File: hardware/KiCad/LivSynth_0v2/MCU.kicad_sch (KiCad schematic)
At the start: 20 parts, among them J16 USB_B_Micro, J19 SWD, SW7 SW_SPDT, U9 STM32F405RGT6, Y1 ABM8-16

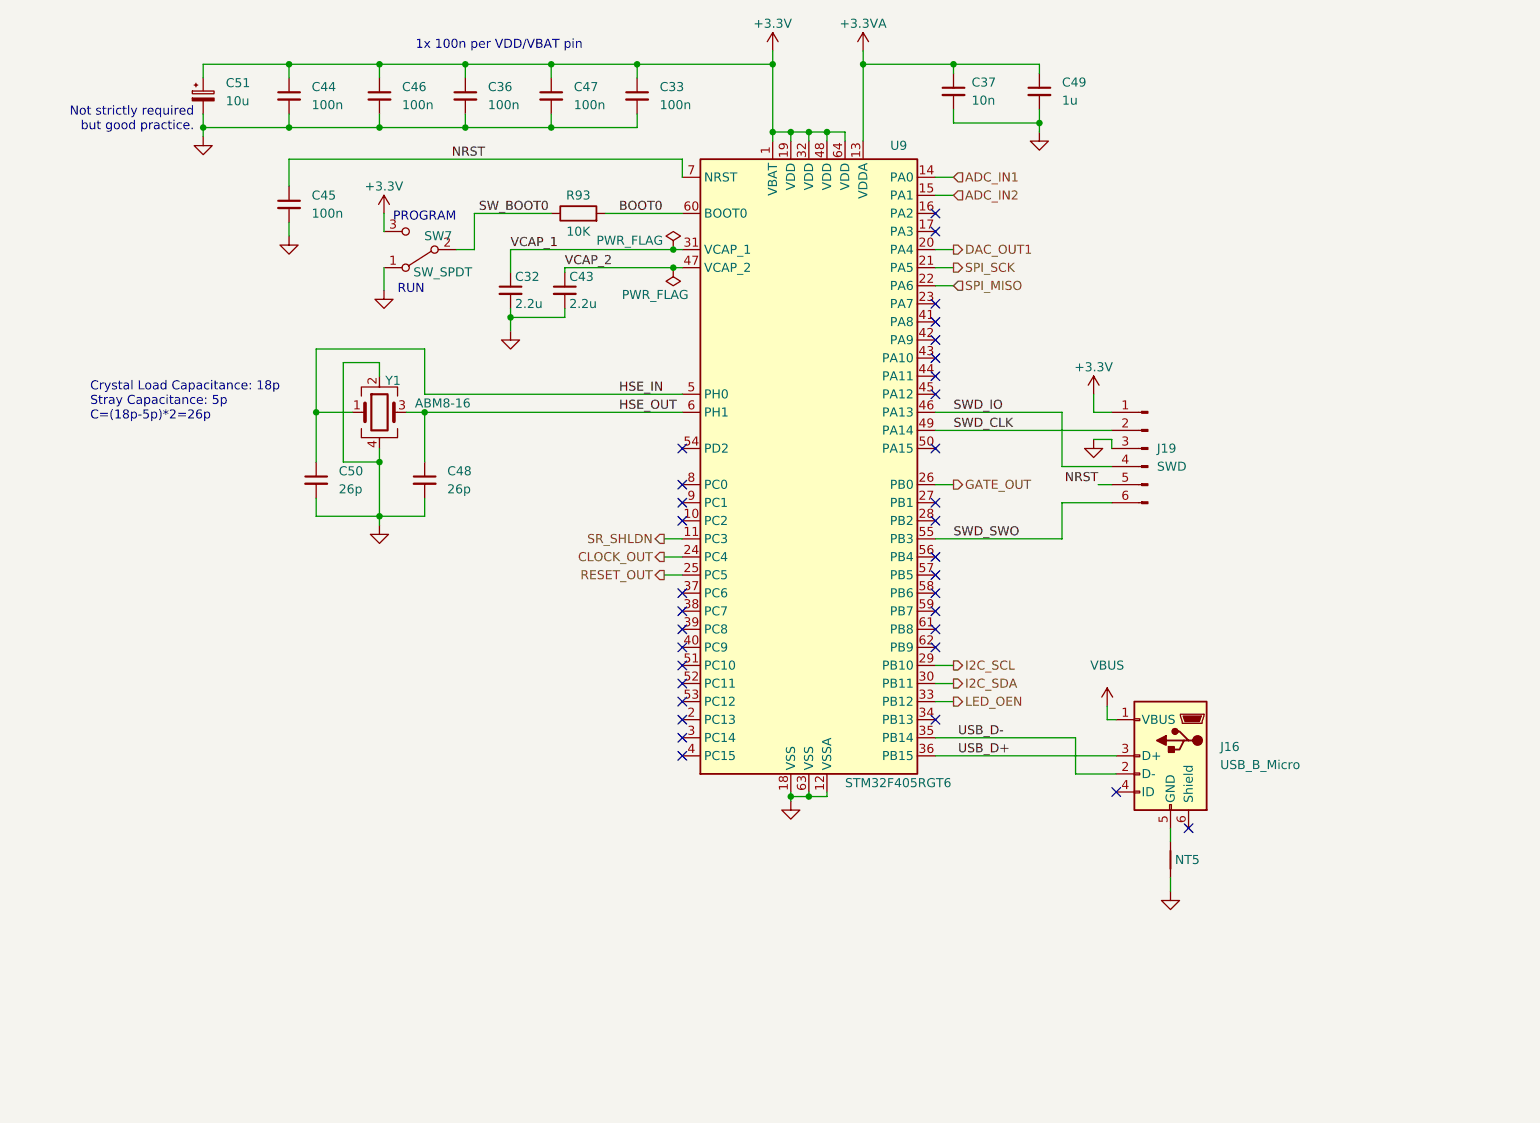
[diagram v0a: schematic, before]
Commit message: Analog redesign:  - Power: Add voltage and current test points  - MCU: use PA11/PA12 for USB DFU interface  - MCU: add NRST reset switch  - Slew: increase portamento cap  - VCO: invert trim pots  - VCF: let resonance kick in earlier  - VCF: invert pots  - VCA: invert trim pot  - EG: full redesign, properly referencing VGND now  - LFO: R61 = 51K  - ModMatrix: add EG attenuverters  - IO: invert pots  - IO: limit output gain for 1W speaker  - IO: connect BTN_SHIFT in gap free order to SR
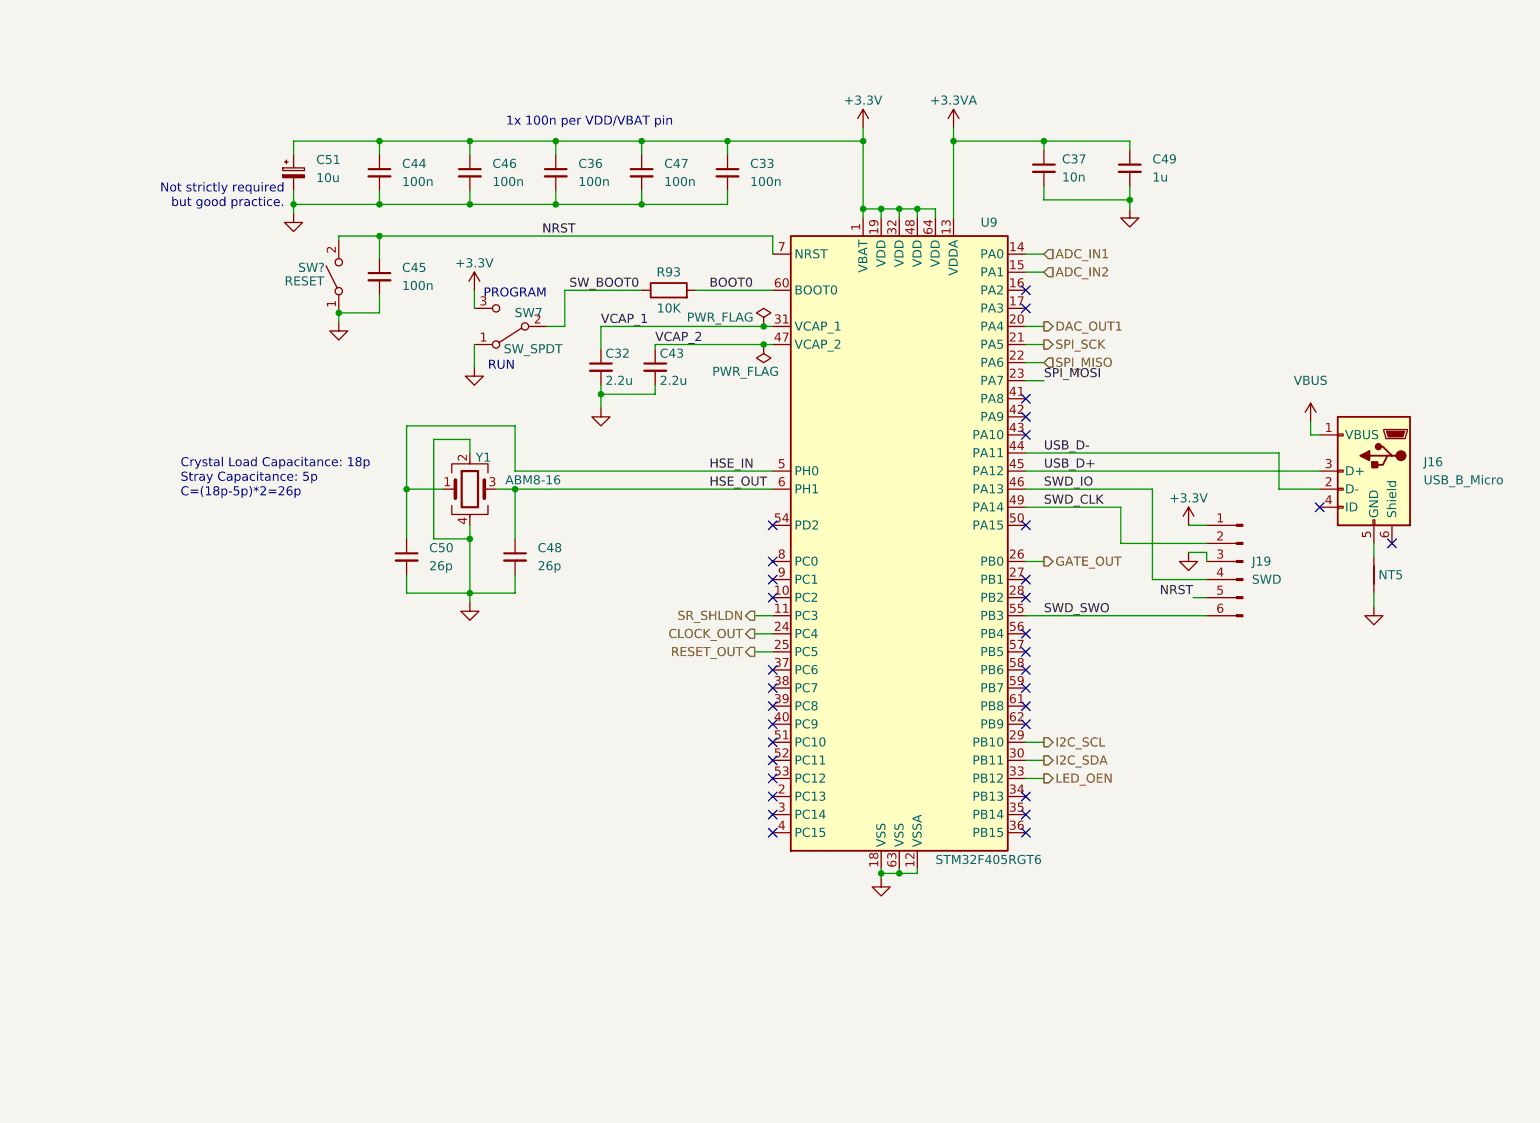
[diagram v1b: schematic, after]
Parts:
- added SW?: RESET, SloBlo:SW_Toggle_MS500C, symbol Switch:SW_SPST
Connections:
- net GND: now also SW?.1 (A)
- net NRST: now also SW?.2 (B)
- net USB_D+: now also U9.45 (PA12); no longer U9.36 (PB15)
- net USB_D-: now also U9.44 (PA11); no longer U9.35 (PB14)
- net SPI_MOSI: now reaches U9.23 (PA7)
- no-connect marks 34 -> 33
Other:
- moved on the sheet: C32, C33, C36, C37, C43, C44, C45, C46, C47, C48, C49, C50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

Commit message: Analog Redesign:  - Power: Build ververse polarity protection using P-Mosfet and Zener Diode      - (https://www.youtube.com/watch?v=Ltx4vovY5Z4 - 1:28)  - Power: Build adjustable buck regulator for 8-9V stable voltage source  - PCB: Add location for order number ("JLCJLCJLCJLC")  - General: Add Tooling Holes for PCB assembly  - PCB: check frontend component layout for symmetry  - VCF: fix sound issues  - PCB: Add SloBlo icon  - PCB: Add switch labels to front side  - EG: test new design  - MCU: Add some debug pins
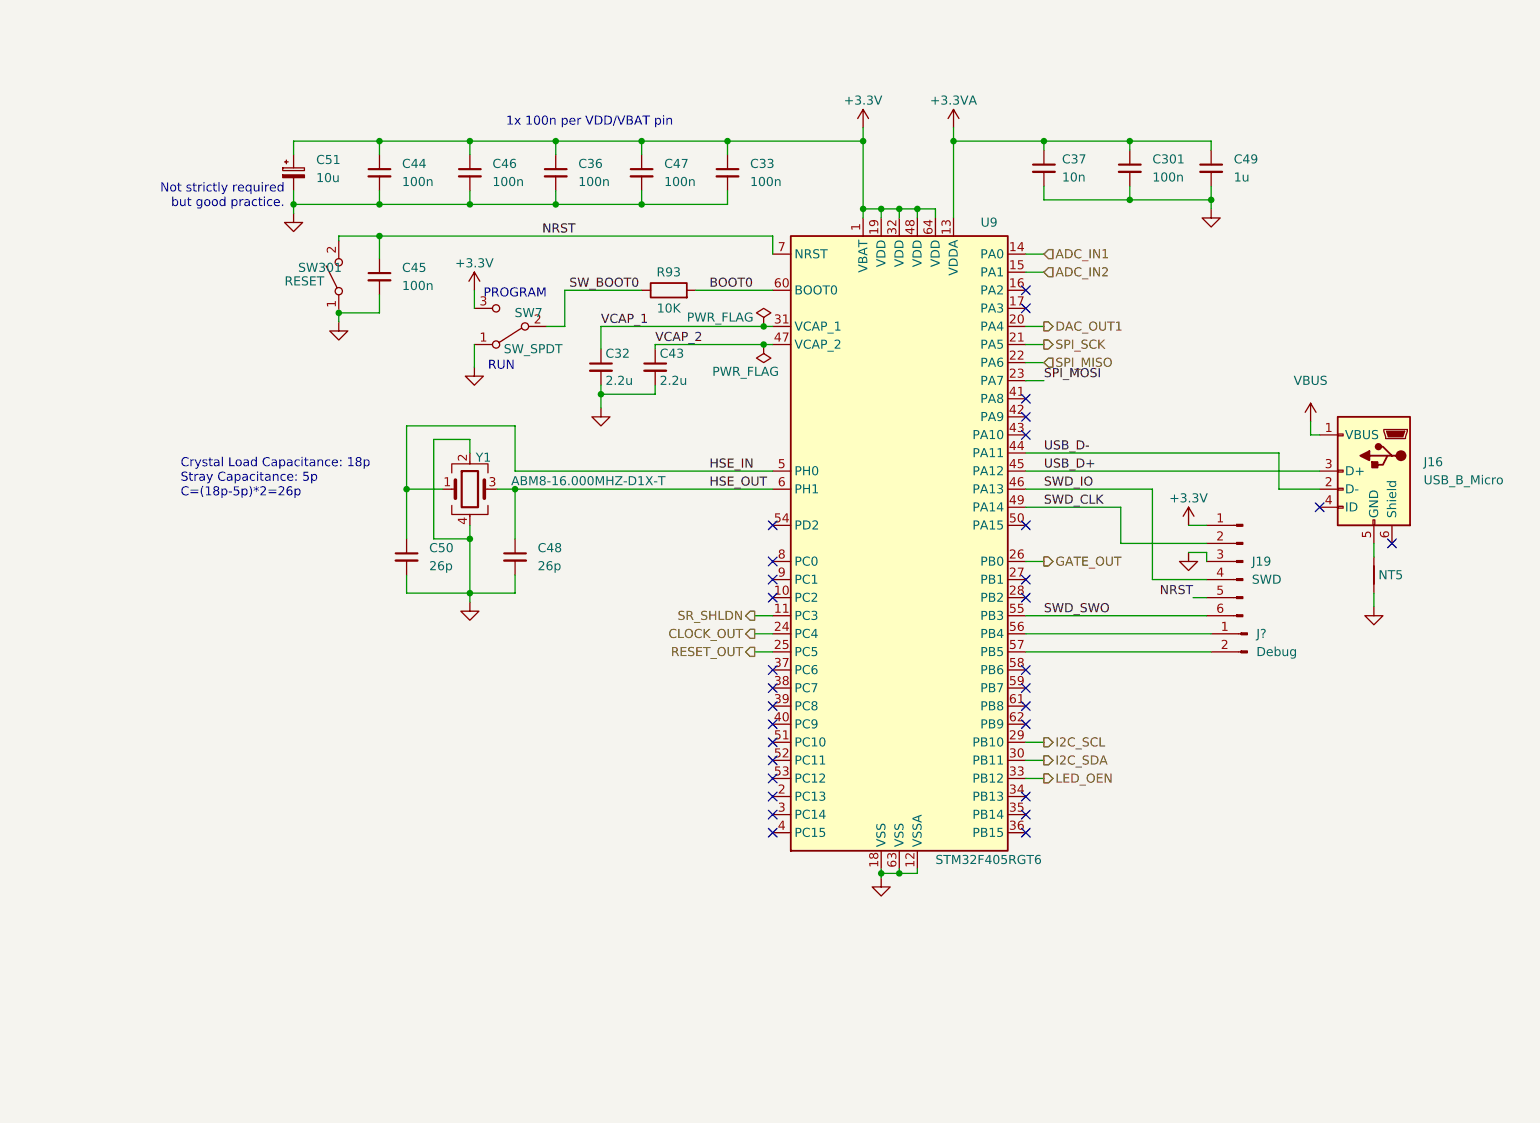
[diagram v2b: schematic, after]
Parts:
- added C301: 100n, Capacitor_THT:C_Rect_L7.2mm_W2.5mm_P5.00mm_FKS2_FKP2_MKS2_MKP2, symbol Device:C_Small
- added J?: Debug, symbol Connector:Conn_01x02_Male
- C32, C43: LCSC (none) -> C268016
- C33, C36, C44, C45, C46, C47: LCSC (none) -> C282518
- U9: LCSC (none) -> C15742
- Y1: value ABM8-16 -> ABM8-16.000MHZ-D1X-T; LCSC (none) -> C1985300
- gave numbers to parts that had none: 1
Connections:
- net +3.3VA: now also C301.1
- net GND: now also C301.2
- net at U9.56 (PB4): now also J?.1 (Pin_1)
- net at U9.57 (PB5): now also J?.2 (Pin_2)
- no-connect marks 33 -> 31
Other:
- moved on the sheet: C49

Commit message: progress 2023-01-21
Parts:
- removed SW301: RESET, SloBlo:SW_Toggle_MS500C, symbol Switch:SW_SPST
- added R301: 10K, Resistor_THT:R_Axial_DIN0207_L6.3mm_D2.5mm_P7.62mm_Horizontal, symbol Device:R
- added SW8: SW_Push, Button_Switch_SMD:SW_SPST_EVQQ2, symbol Switch:SW_Push
- J301: renamed from J?; footprint (none) -> Connector_PinHeader_2.54mm:PinHeader_1x02_P2.54mm_Vertical
- NT5: footprint NetTie:NetTie-2_SMD_Pad2.0mm -> NetTie:NetTie-2_SMD_Pad0.5mm
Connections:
- net ADC_IN2: now also U9.27 (PB1); no longer U9.15 (PA1)
- net GATE_OUT: now also U9.23 (PA7); no longer U9.26 (PB0)
- net GND: now also R301.2, SW8.1
- net HSE_IN: now also Y1.3; no longer Y1.1
- net HSE_OUT: now also Y1.1; no longer Y1.3
- net I2C_SCL: now also U9.58 (PB6); no longer U9.29 (PB10)
- net I2C_SDA: now also U9.59 (PB7); no longer U9.30 (PB11)
- net NRST: now also SW8.2
- net SPI_MOSI: now also U9.53 (PC12), R301.1; no longer U9.23 (PA7)
- net at U9.56 (PB4): no longer J301.1 (Pin_1)
- net at U9.57 (PB5): no longer J301.2 (Pin_2)
- net DBG1: now reaches U9.35 (PB14)
- net DBG1: now also J301.1 (Pin_1)
- net DBG2: now reaches U9.36 (PB15)
- net DBG2: now also J301.2 (Pin_2)
- net SR_SPI_SCK: now reaches U9.51 (PC10)
- net SR_SPI_MISO: now reaches U9.52 (PC11)
- net SPI_MISO: no longer names the net of U9.22 (PA6)
- net SPI_SCK: no longer names the net of U9.21 (PA5)
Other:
- note added: "Reset"
- moved on the sheet: J301

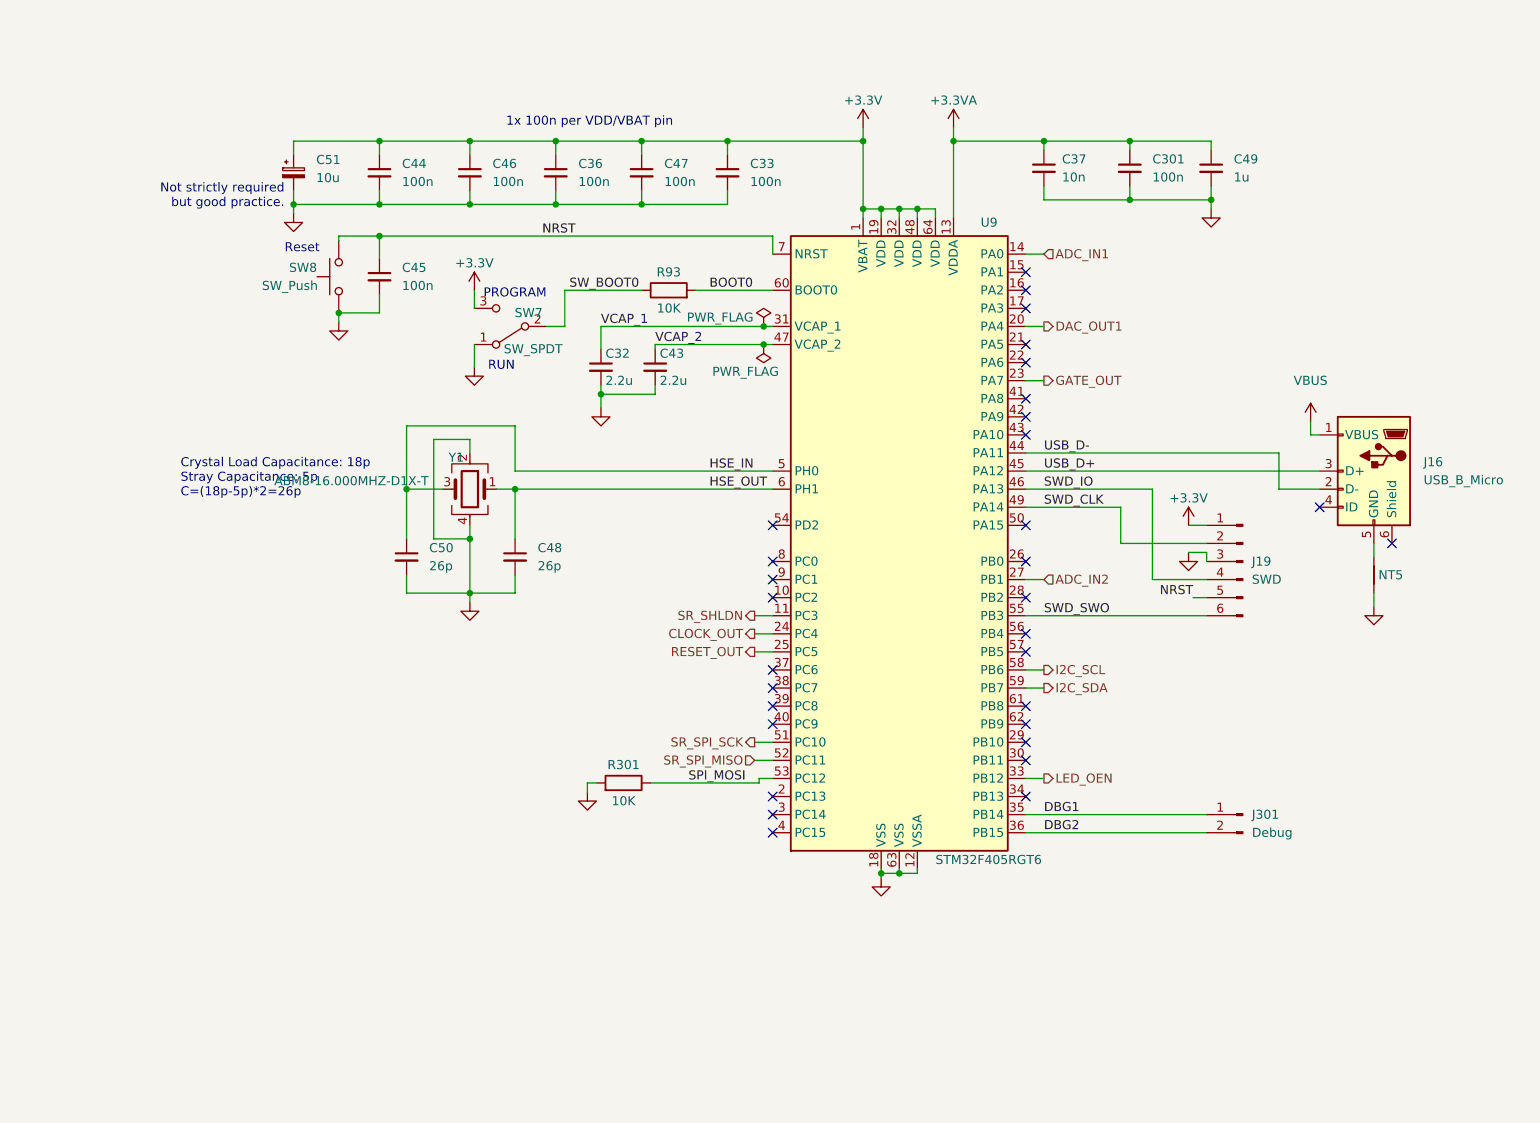
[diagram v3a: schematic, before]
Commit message: DRC: no severe errors
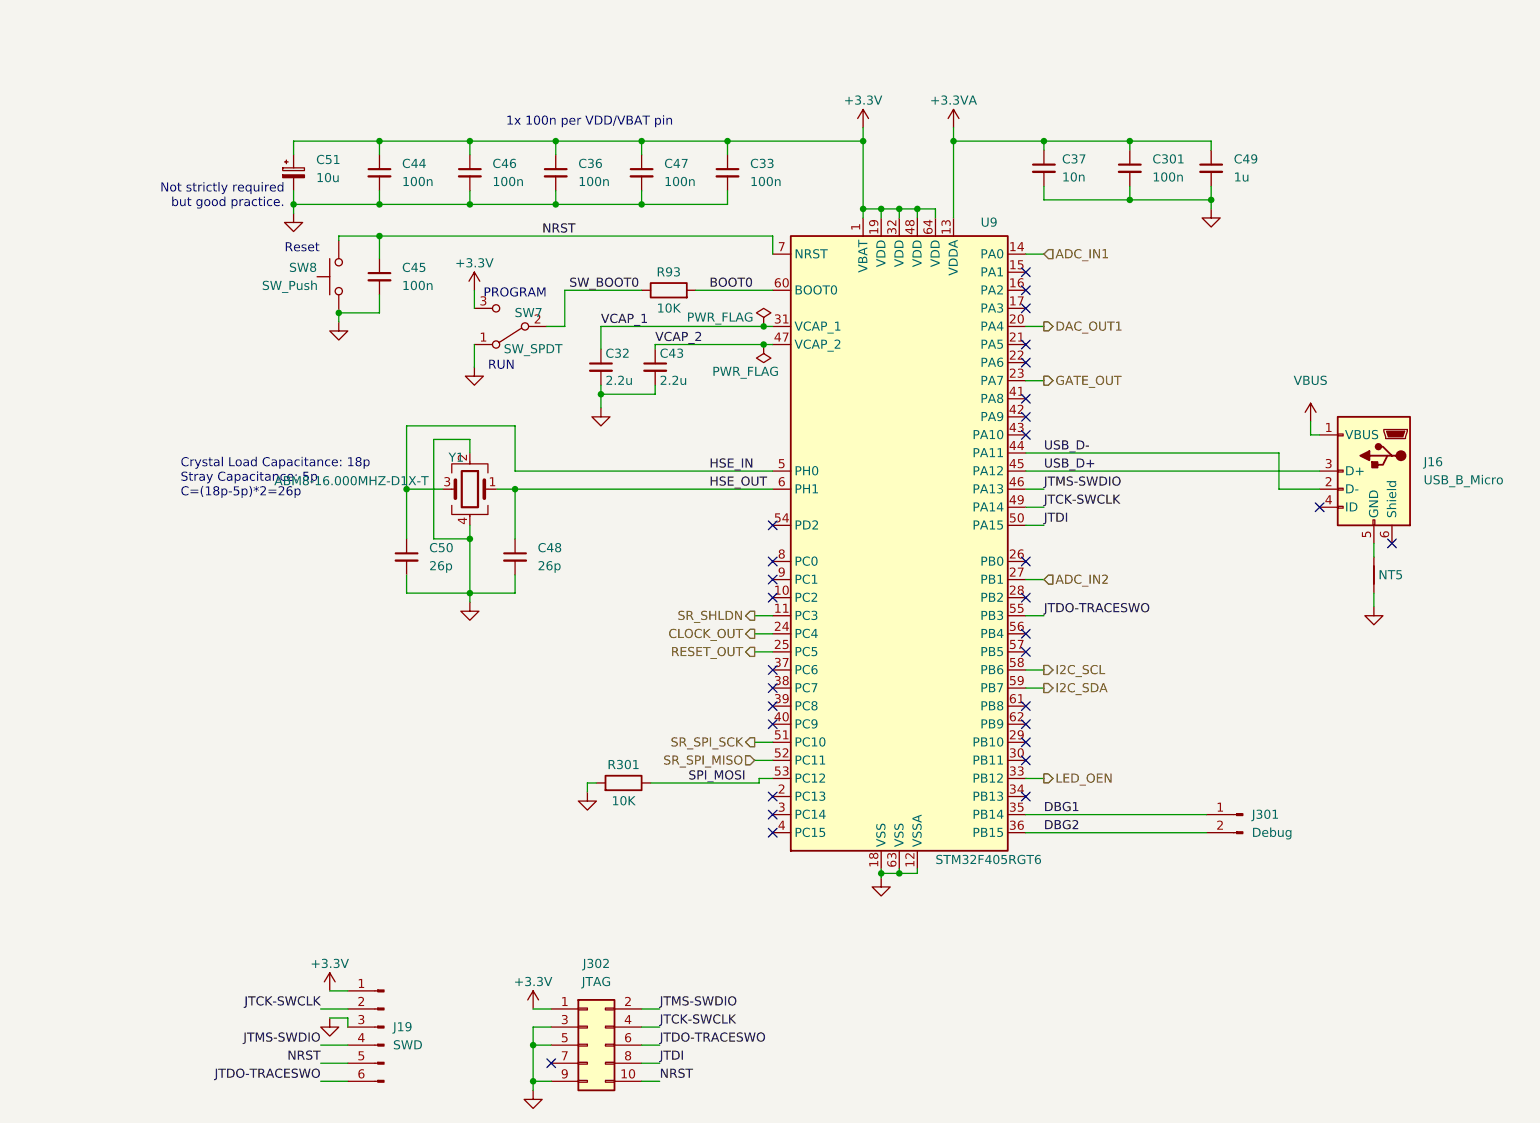
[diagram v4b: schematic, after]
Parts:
- added J302: JTAG, Connector_PinHeader_1.27mm:PinHeader_2x05_P1.27mm_Vertical, symbol Connector_Generic:Conn_02x05_Odd_Even
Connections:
- net +3.3V: now also J302.1 (Pin_1)
- net GND: now also J302.3 (Pin_3), J302.5 (Pin_5), J302.9 (Pin_9)
- net NRST: now also J302.10 (Pin_10)
- net JTDI: now reaches U9.50 (PA15)
- net JTDI: now also J302.8 (Pin_8)
- net SWD_CLK renamed JTCK-SWCLK
- net JTCK-SWCLK: now also J302.4 (Pin_4)
- net SWD_IO renamed JTMS-SWDIO
- net JTMS-SWDIO: now also J302.2 (Pin_2)
- net SWD_SWO renamed JTDO-TRACESWO
- net JTDO-TRACESWO: now also J302.6 (Pin_6)
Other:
- moved on the sheet: J19
